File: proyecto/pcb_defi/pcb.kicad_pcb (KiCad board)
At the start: 2 copper layers, 59 parts, among them J1 pines de senspores, J2 pines de gps, J3 Conn_01x03_Pin, J5 pines de gps, J6 pines de gps, J7 pines de senspores, J8 pines de gps, Q2 AON7423, U1 module_mpu6050, U3 module_bme680, U4 module_vl53L0x-v2, U5 ESP32-CAM, U6 ESP32-DevKitC, U7 ZC323200

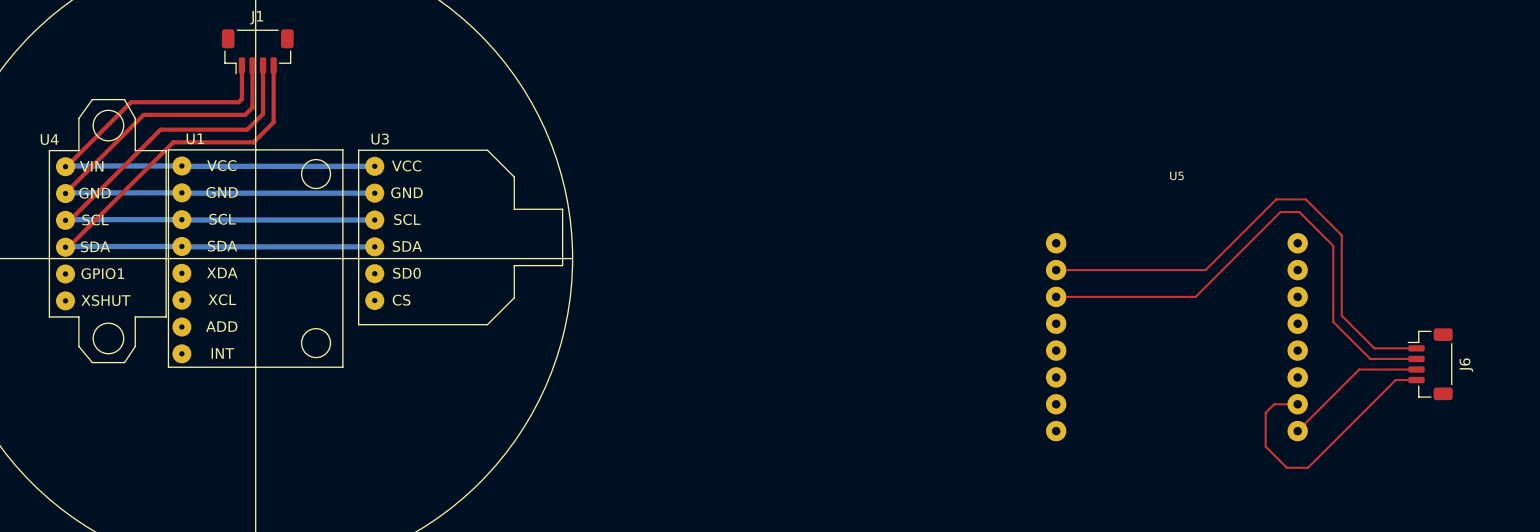
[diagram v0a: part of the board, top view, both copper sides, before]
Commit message: integracion entre horizonte artificial y guardado de datos para que no se pierdan cada ves que se reinicia el server,  boton para  descargar los archivos csv desde la pagina
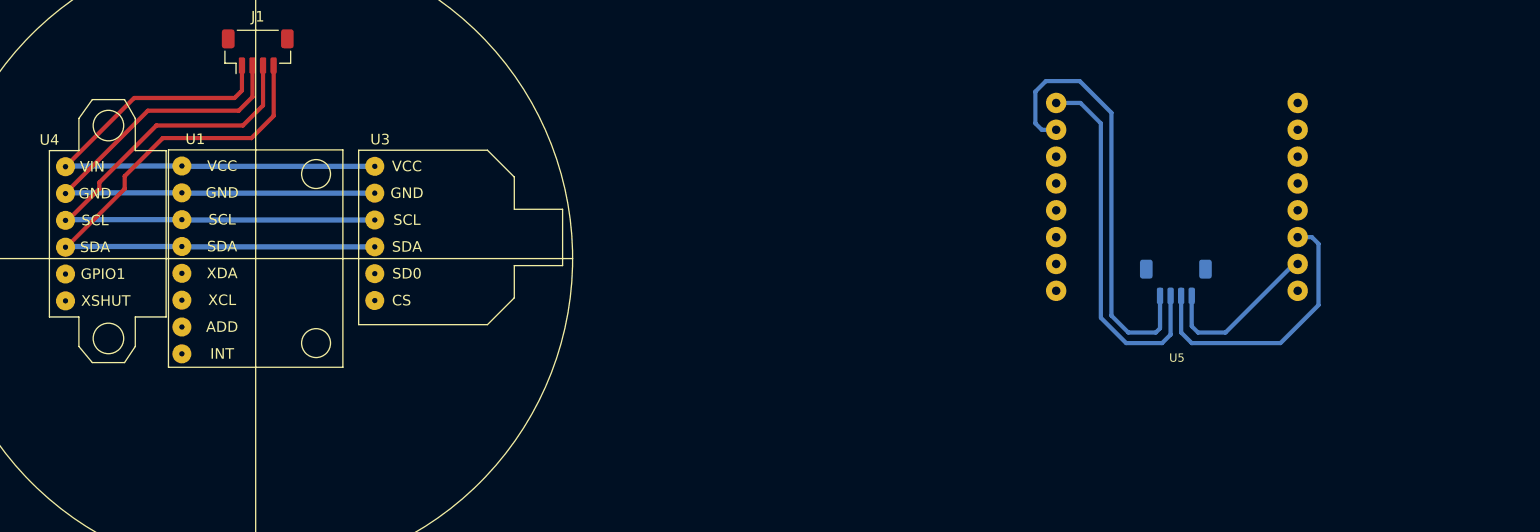
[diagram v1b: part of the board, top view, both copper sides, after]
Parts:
- J6: moved to B.Cu
- moved J6 25.3 mm to (147.3, 139.0), turned to 180 degrees
- moved U5 17.2 mm to (147.4, 146.2), turned to 180 degrees
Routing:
- net Net-(J6-Pin_1): track 47.2 -> 15.8 mm
- net Net-(J6-Pin_3): track 13.7 -> 35.0 mm
- net Net-(J6-Pin_2): track 47.4 -> 26.4 mm
- net Net-(J6-Pin_4): track 25.1 -> 41.8 mm
- net Net-(J1-Pin_2): track 55.0 -> 54.1 mm
- net Net-(J1-Pin_3): track 57.6 -> 56.9 mm
